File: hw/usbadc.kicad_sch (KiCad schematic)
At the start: 14 parts, among them U6 PCA9306DC1, U8 24AA0x, X1 ECS-2520MV-260-CN-TR

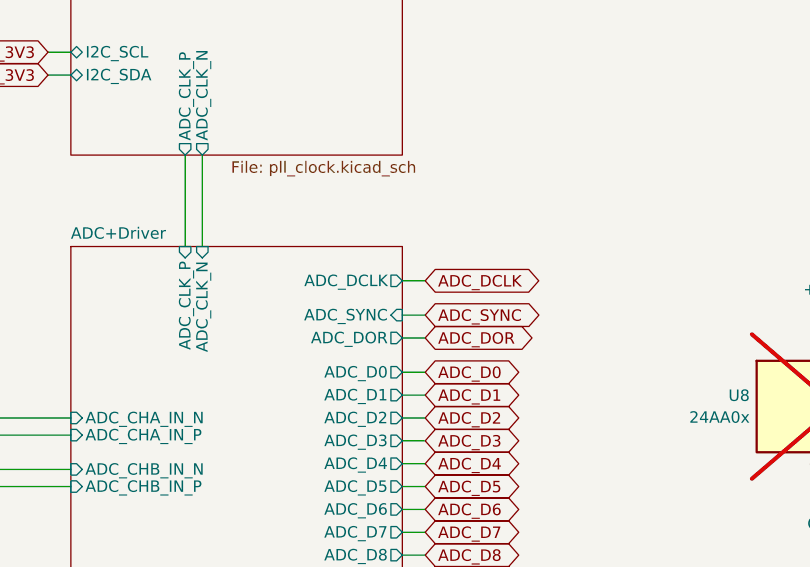
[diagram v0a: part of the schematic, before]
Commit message: Modified DAC resistors/range; connect + pull-up ADC SHDN
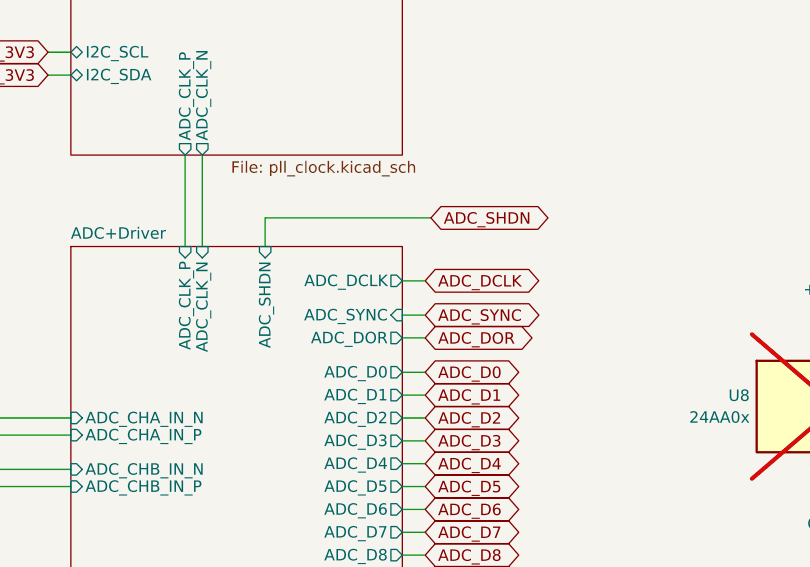
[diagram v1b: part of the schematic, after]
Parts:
- R117, R123, U8: now left out of the parts list
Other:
- sheet ADC+Driver ports: added ADC_SHDN; removed none
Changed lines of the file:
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@@
+    (stroke (width 0) (type default))
+  )
+  (wire (pts (xy 153.035 107.95) (xy 171.45 107.95))
     (stroke (width 0) (type default))
   )
@@
   )
   (wire (pts (xy 146.685 54.61) (xy 146.685 55.88))
+    (stroke (width 0) (type default))
+  )
+  (wire (pts (xy 153.035 111.125) (xy 153.035 107.95))
     (stroke (width 0) (type default))
   )
@@
     )
   )
+  (global_label "ADC_SHDN" (shape bidirectional) (at 171.45 107.95 0) (fields_autoplaced)
+    (effects (font (size 1.27 1.27)) (justify left))
+    (property "Intersheetrefs" "${INTERSHEET_REFS}" (at 184.4702 107.95 0)
+      (effects (font (size 1.27 1.27)) (justify left) hide)
+    )
+  )
   (global_label "ULPI_DIR" (shape bidirectional) (at 50.165 74.295 180) (fields_autoplaced)
     (effects (font (size 1.27 1.27)) (justify right))
@@
   )
   (symbol (lib_id "Device:R_Small") (at 177.165 69.85 0) (unit 1)
-    (in_bom yes) (on_board yes) (dnp yes)
+    (in_bom no) (on_board yes) (dnp yes)
     (property "Reference" "R117" (at 178.6636 68.6816 0)
       (effects (font (size 1.27 1.27)) (justify left))
@@
   )
   (symbol (lib_id "Device:R_Small") (at 85.725 36.195 180) (unit 1)
-    (in_bom yes) (on_board yes) (dnp yes)
+    (in_bom no) (on_board yes) (dnp yes)
     (property "Reference" "R123" (at 84.2264 37.3634 0)
       (effects (font (size 1.27 1.27)) (justify left))
@@
   )
   (symbol (lib_id "fmc:24AA0x") (at 215.265 128.905 0) (unit 1)
-    (in_bom yes) (on_board yes) (dnp yes) (fields_autoplaced)
+    (in_bom no) (on_board yes) (dnp yes) (fields_autoplaced)
     (property "Reference" "U8" (at 206.883 127.6929 0)
       (effects (font (size 1.27 1.27)) (justify right))
@@
       (effects (font (size 1.27 1.27)) (justify left))
     )
-    (instances
+    (pin "ADC_SHDN" input (at 153.035 111.125 90)
+      (effects (font (size 1.27 1.27)) (justify right))
+    )
+    (instances

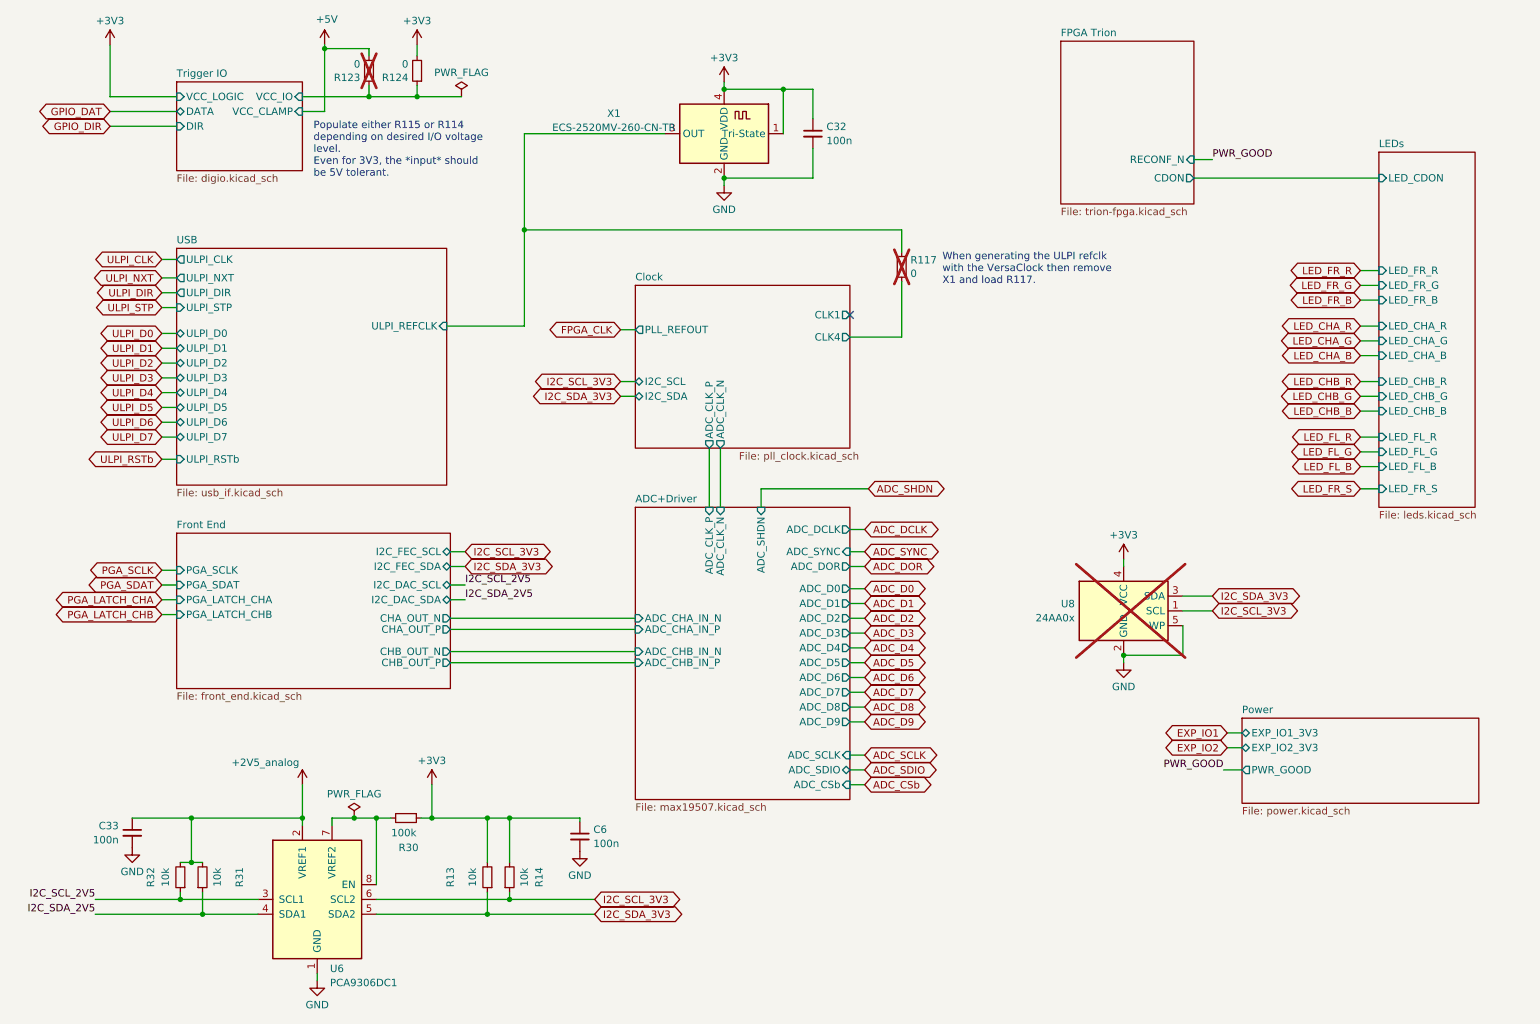
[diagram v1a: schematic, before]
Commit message: renaming, comments, part/vendor and other cosmetics (no pcb change)
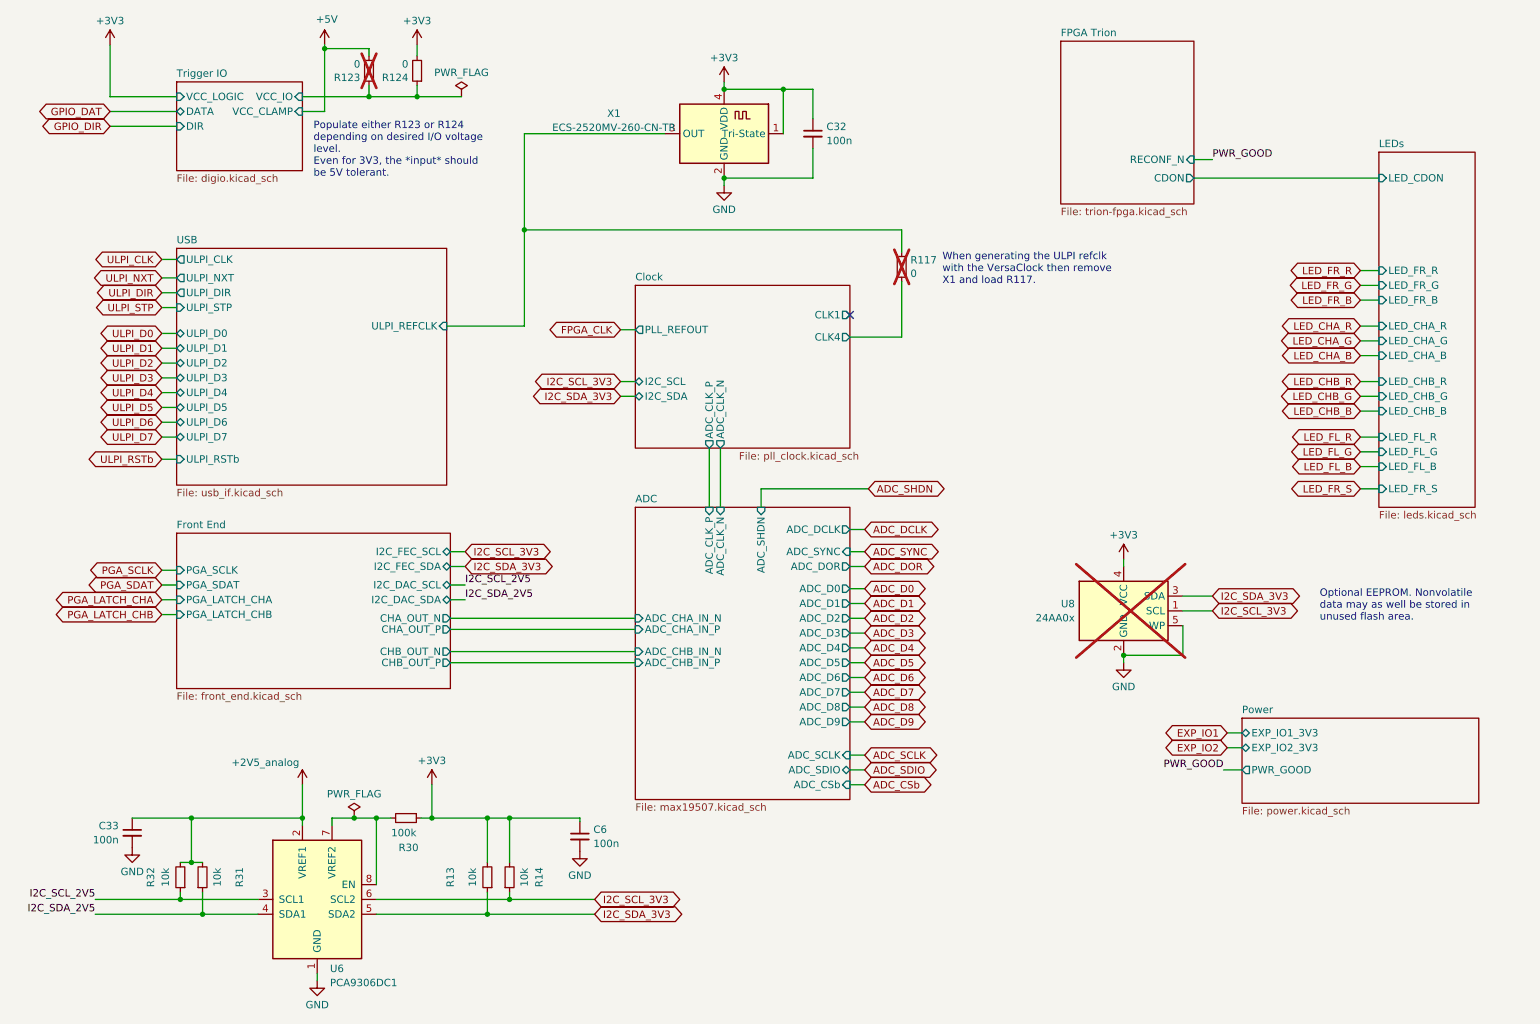
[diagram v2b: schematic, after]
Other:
- sheet ADC+Driver renamed ADC
- note added: "Optional EEPROM. Nonvolatile data may as well be stored in unused flash area."
- note added: "Populate either R123 or R124 depending on desired I/O voltage level. Even for 3V3, the *input* should be 5V tolerant."
- note removed: "Populate either R115 or R114 depending on desired I/O voltage level. Even for 3V3, the *input* should be 5V tolerant."
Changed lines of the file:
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@@
     (stroke (width 0) (type default))
+  )
+  (text "Optional EEPROM. Nonvolatile\ndata may as well be stored in\nunused flash area."
+    (at 248.92 130.81 0)
+    (effects (font (size 1.27 1.27)) (justify left bottom))
   )
   (text "When generating the ULPI refclk\nwith the VersaClock then remove\nX1 and load R117."
@@
     (effects (font (size 1.27 1.27)) (justify left bottom))
   )
-  (text "Populate either R115 or R114\ndepending on desired I/O voltage\nlevel.\nEven for 3V3, the *input* should\nbe 5V tolerant."
+  (text "Populate either R123 or R124\ndepending on desired I/O voltage\nlevel.\nEven for 3V3, the *input* should\nbe 5V tolerant."
     (at 76.2 54.61 0)
     (effects (font (size 1.27 1.27)) (justify left bottom))
@@
     (stroke (width 0) (type solid))
     (fill (color 0 0 0 0.0000))
-    (property "Sheetname" "ADC+Driver" (at 131.445 110.4134 0)
+    (property "Sheetname" "ADC" (at 131.445 110.4134 0)
       (effects (font (size 1.27 1.27)) (justify left bottom))
     )

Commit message: added pll clock in divider from BNC, several pull-resistors
pull-resistors permit distinguishing board revisions.
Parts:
- U6: footprint Package_SO:VSSOP-8_2.4x2.1mm_P0.5mm -> Package_SO:VSSOP-8_2.3x2mm_P0.5mm
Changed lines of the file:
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@@
 			)
 		)
-		(property "Footprint" "Package_SO:VSSOP-8_2.4x2.1mm_P0.5mm"
+		(property "Footprint" "Package_SO:VSSOP-8_2.3x2mm_P0.5mm"
 			(at 66.675 169.545 0)
 			(effects

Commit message: updated parts assignments
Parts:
- R117, R123, R124: Manufacturer (none) -> Stackpole; Part (none) -> RMCF0603ZT0R00
- R13, R14, R31, R32: Manufacturer (none) -> Stackpole; Part (none) -> RMCF0603FT10K0
- R30: Manufacturer (none) -> Stackpole; Part (none) -> RMCF0603FT100K
- U6: Manufacturer (none) -> TI; Part (none) -> PCA9306TDCURQ1
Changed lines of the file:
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@@
 			)
 		)
-		(property "Part" ""
+		(property "Part" "RMCF0603FT10K0"
 			(at 53.34 174.625 90)
 			(effects
@@
 			)
 		)
-		(property "Manufacturer" ""
+		(property "Manufacturer" "Stackpole"
 			(at 53.34 174.625 90)
 			(effects
@@
 			)
 		)
-		(property "Part" ""
+		(property "Part" " RMCF0603ZT0R00"
 			(at 177.165 69.85 0)
 			(effects
@@
 			)
 		)
-		(property "Manufacturer" ""
+		(property "Manufacturer" "Stackpole"
 			(at 177.165 69.85 0)
 			(effects
@@
 			)
 		)
-		(property "Part" ""
+		(property "Part" "  RMCF0603ZT0R00"
 			(at 93.98 36.195 0)
 			(effects
@@
 			)
 		)
-		(property "Manufacturer" ""
+		(property "Manufacturer" "Stackpole"
 			(at 93.98 36.195 0)
 			(effects
@@
 			)
 		)
+		(property "Manufacturer" "TI"
+			(at 76.835 178.435 0)
+			(effects
+				(font
+					(size 1.27 1.27)
+				)
+				(hide yes)
+			)
+		)
+		(property "Part" "PCA9306TDCURQ1"
+			(at 76.835 178.435 0)
+			(effects
+				(font
+					(size 1.27 1.27)
+				)
+				(hide yes)
+			)
+		)
 		(pin "7"
 		)
@@
 			)
 		)
-		(property "Part" ""
+		(property "Part" "RMCF0603FT10K0"
 			(at 109.855 174.625 90)
 			(effects
@@
 			)
 		)
-		(property "Manufacturer" ""
+		(property "Manufacturer" "Stackpole"
 			(at 109.855 174.625 90)
 			(effects
@@
 			)
 		)
-		(property "Part" ""
+		(property "Part" " RMCF0603ZT0R00"
 			(at 85.725 36.195 0)
 			(effects
@@
 			)
 		)
-		(property "Manufacturer" ""
+		(property "Manufacturer" "Stackpole"
 			(at 85.725 36.195 0)
 			(effects
@@
 			)
 		)
-		(property "Part" ""
+		(property "Part" "RMCF0603FT10K0"
 			(at 106.045 174.625 90)
 			(effects
@@
 			)
 		)
-		(property "Manufacturer" ""
+		(property "Manufacturer" "Stackpole"
 			(at 106.045 174.625 90)
 			(effects
@@
 			)
 		)
-		(property "Part" ""
+		(property "Part" "RMCF0603FT100K"
 			(at 92.075 164.465 0)
 			(effects
@@
 			)
 		)
-		(property "Manufacturer" ""
+		(property "Manufacturer" "Stackpole"
 			(at 92.075 164.465 0)
 			(effects
@@
 			)
 		)
-		(property "Part" ""
+		(property "Part" "RMCF0603FT10K0"
 			(at 57.15 174.625 90)
 			(effects
@@
 			)
 		)
-		(property "Manufacturer" ""
+		(property "Manufacturer" "Stackpole"
 			(at 57.15 174.625 90)
 			(effects
